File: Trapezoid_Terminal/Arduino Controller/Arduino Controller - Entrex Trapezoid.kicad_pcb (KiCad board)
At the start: 2 copper layers, 114 x 87 mm, 18 parts, among them J1 Conn_01x19, J10 Conn_01x04, J2 Conn_01x04, J3 Conn_01x08, J4 Conn_01x08, J5 Conn_01x06, J6 Conn_01x04, J8 Conn_01x19, J9 Logic 8 CH, U1 74LS04

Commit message: Controller
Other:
- board text added: "Entrex {dblquote}Trapezoid{dblquote} Data/Terminal Controller"
- board text removed: "Entrex {dblquote}Trapezoid{dblquote} Data/Terminal Interface"
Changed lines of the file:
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@@
     (effects (font (size 1 1) (thickness 0.15)))
   )
-  (gr_text "Entrex {dblquote}Trapezoid{dblquote} Data/Terminal Interface" (at 51.181 64.262) (layer "F.SilkS")
+  (gr_text "Entrex {dblquote}Trapezoid{dblquote} Data/Terminal Controller" (at 51.181 64.262) (layer "F.SilkS")
     (effects (font (size 3 3) (thickness 0.5) bold) (justify left bottom))
   )

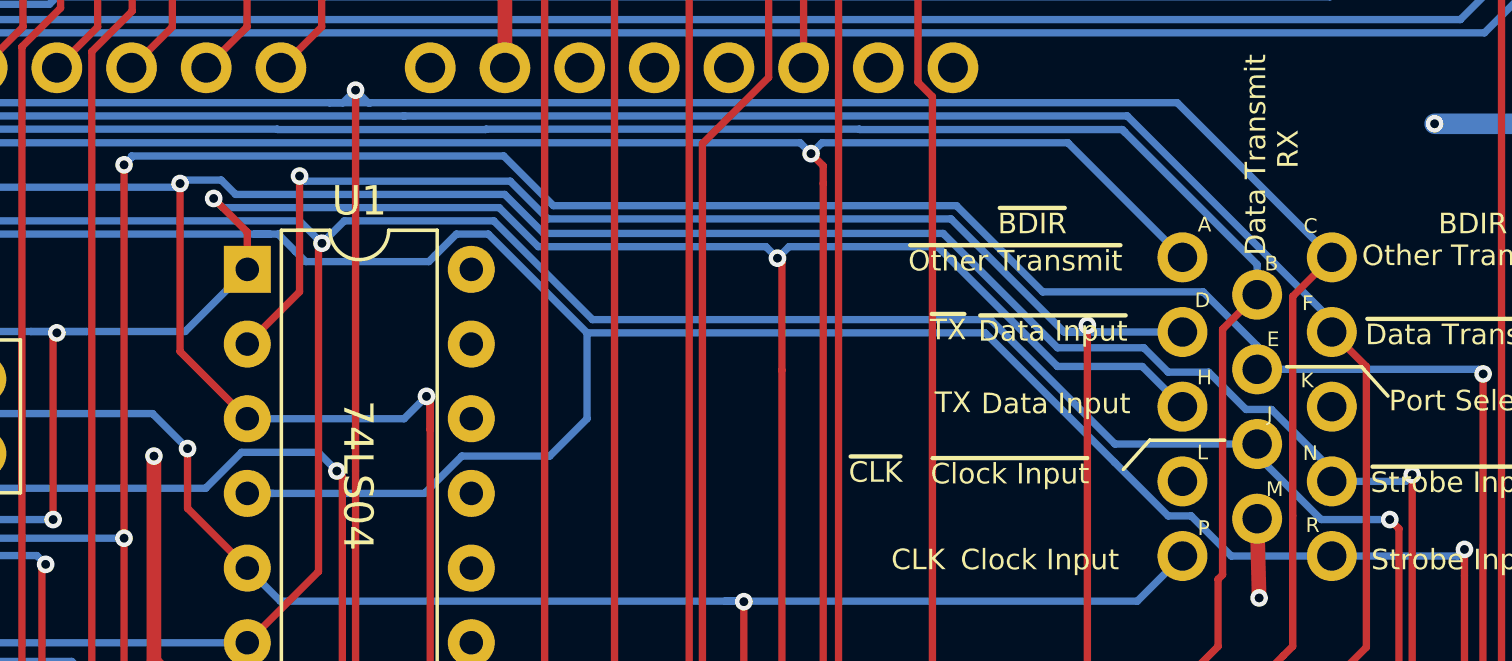
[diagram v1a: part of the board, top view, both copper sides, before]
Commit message: Trapezoid Arduino KiCad
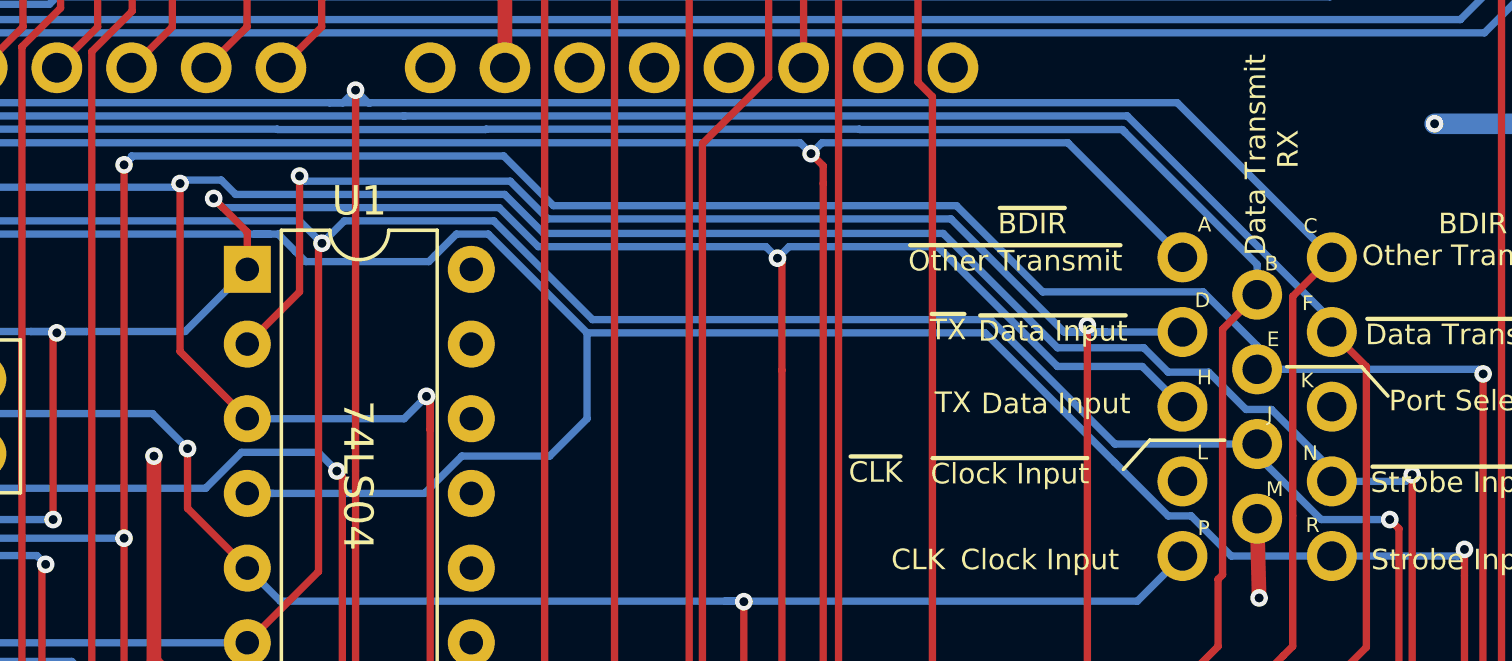
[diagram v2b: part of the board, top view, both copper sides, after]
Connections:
- J9 pad 5: Strobe Input -> ~{Strobe Input}
- U1 pad 3: Strobe Input -> ~{Strobe Input}
- U1 pad 4: ~{Strobe Input} -> Strobe Input
- XA1 pad D7: Strobe Input -> ~{Strobe Input}
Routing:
- net Strobe Input: track 149.0 -> 113.3 mm, vias 4 -> 3
- net ~{Strobe Input}: track 113.3 -> 149.0 mm, vias 3 -> 4
